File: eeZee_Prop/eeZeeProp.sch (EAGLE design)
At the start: 33 parts, among them Q1 5MHz, Q2 2N3904SMD, SW1 RESET, U1 P8X32A-Q44, U2 24LC256-I/ST, U3 NCP1117 3V3

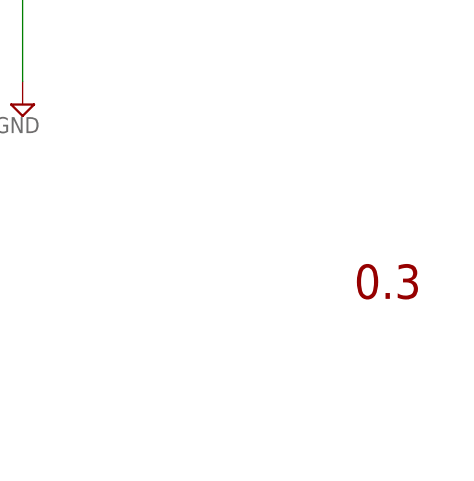
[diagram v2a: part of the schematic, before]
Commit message: Enlarged pads for SOT-23 and SOD123F for easier hand assembly. Slight tweaks to traces.
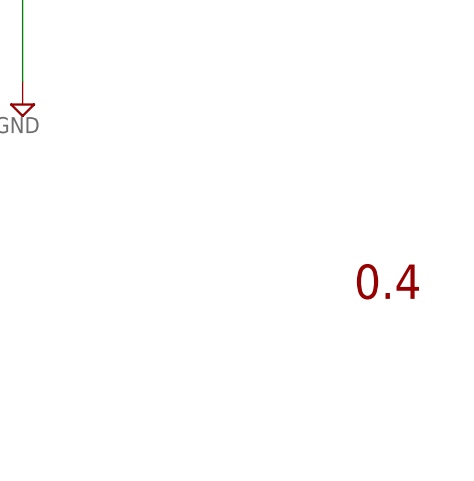
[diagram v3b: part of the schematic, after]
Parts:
- C7: PARTNO (none) -> 0603YC104KAT2A
- Q2: PARTNO (none) -> MMBT3904LT3G
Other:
- note added: "0.4"
- note removed: "0.3"
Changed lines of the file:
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@@
 <grid distance="0.1" unitdist="inch" unit="inch" style="lines" multiple="1" display="no" altdistance="0.01" altunitdist="inch" altunit="inch"/>
 <layers>
-<layer number="1" name="Top" color="4" fill="1" visible="yes" active="no"/>
-<layer number="16" name="Bottom" color="1" fill="1" visible="yes" active="no"/>
-<layer number="17" name="Pads" color="2" fill="1" visible="yes" active="no"/>
-<layer number="18" name="Vias" color="2" fill="1" visible="yes" active="no"/>
-<layer number="19" name="Unrouted" color="6" fill="1" visible="yes" active="no"/>
-<layer number="20" name="Dimension" color="15" fill="1" visible="yes" active="no"/>
-<layer number="21" name="tPlace" color="7" fill="1" visible="yes" active="no"/>
-<layer number="22" name="bPlace" color="7" fill="1" visible="yes" active="no"/>
-<layer number="23" name="tOrigins" color="15" fill="1" visible="yes" active="no"/>
-<layer number="24" name="bOrigins" color="15" fill="1" visible="yes" active="no"/>
-<layer number="25" name="tNames" color="7" fill="1" visible="yes" active="no"/>
-<layer number="26" name="bNames" color="7" fill="1" visible="yes" active="no"/>
-<layer number="27" name="tValues" color="7" fill="1" visible="yes" active="no"/>
-<layer number="28" name="bValues" color="7" fill="1" visible="yes" active="no"/>
+<layer number="1" name="Top" color="4" fill="1" visible="no" active="no"/>
+<layer number="16" name="Bottom" color="1" fill="1" visible="no" active="no"/>
+<layer number="17" name="Pads" color="2" fill="1" visible="no" active="no"/>
+<layer number="18" name="Vias" color="2" fill="1" visible="no" active="no"/>
+<layer number="19" name="Unrouted" color="6" fill="1" visible="no" active="no"/>
+<layer number="20" name="Dimension" color="15" fill="1" visible="no" active="no"/>
+<layer number="21" name="tPlace" color="7" fill="1" visible="no" active="no"/>
+<layer number="22" name="bPlace" color="7" fill="1" visible="no" active="no"/>
+<layer number="23" name="tOrigins" color="15" fill="1" visible="no" active="no"/>
+<layer number="24" name="bOrigins" color="15" fill="1" visible="no" active="no"/>
+<layer number="25" name="tNames" color="7" fill="1" visible="no" active="no"/>
+<layer number="26" name="bNames" color="7" fill="1" visible="no" active="no"/>
+<layer number="27" name="tValues" color="7" fill="1" visible="no" active="no"/>
+<layer number="28" name="bValues" color="7" fill="1" visible="no" active="no"/>
 <layer number="29" name="tStop" color="7" fill="3" visible="no" active="no"/>
 <layer number="30" name="bStop" color="7" fill="6" visible="no" active="no"/>
@@
 <layer number="35" name="tGlue" color="7" fill="4" visible="no" active="no"/>
 <layer number="36" name="bGlue" color="7" fill="5" visible="no" active="no"/>
-<layer number="37" name="tTest" color="7" fill="1" visible="yes" active="no"/>
-<layer number="38" name="bTest" color="7" fill="1" visible="yes" active="no"/>
+<layer number="37" name="tTest" color="7" fill="1" visible="no" active="no"/>
+<layer number="38" name="bTest" color="7" fill="1" visible="no" active="no"/>
 <layer number="39" name="tKeepout" color="4" fill="11" visible="no" active="no"/>
 <layer number="40" name="bKeepout" color="1" fill="11" visible="no" active="no"/>
@@
 <layer number="44" name="Drills" color="7" fill="1" visible="no" active="no"/>
 <layer number="45" name="Holes" color="7" fill="1" visible="no" active="no"/>
-<layer number="46" name="Milling" color="3" fill="1" visible="yes" active="no"/>
-<layer number="47" name="Measures" color="7" fill="1" visible="yes" active="no"/>
-<layer number="48" name="Document" color="7" fill="1" visible="yes" active="no"/>
-<layer number="49" name="Reference" color="7" fill="1" visible="yes" active="no"/>
-<layer number="50" name="dxf" color="7" fill="1" visible="yes" active="no"/>
-<layer number="51" name="tDocu" color="7" fill="1" visible="yes" active="no"/>
-<layer number="52" name="bDocu" color="7" fill="1" visible="yes" active="no"/>
-<layer number="53" name="tGND_GNDA" color="7" fill="9" visible="yes" active="no"/>
-<layer number="54" name="bGND_GNDA" color="1" fill="9" visible="yes" active="no"/>
-<layer number="56" name="wert" color="7" fill="1" visible="yes" active="no"/>
+<layer number="46" name="Milling" color="3" fill="1" visible="no" active="no"/>
+<layer number="47" name="Measures" color="7" fill="1" visible="no" active="no"/>
+<layer number="48" name="Document" color="7" fill="1" visible="no" active="no"/>
+<layer number="49" name="Reference" color="7" fill="1" visible="no" active="no"/>
+<layer number="50" name="dxf" color="7" fill="1" visible="no" active="no"/>
+<layer number="51" name="tDocu" color="7" fill="1" visible="no" active="no"/>
+<layer number="52" name="bDocu" color="7" fill="1" visible="no" active="no"/>
+<layer number="53" name="tGND_GNDA" color="7" fill="9" visible="no" active="no"/>
+<layer number="54" name="bGND_GNDA" color="1" fill="9" visible="no" active="no"/>
+<layer number="56" name="wert" color="7" fill="1" visible="no" active="no"/>
 <layer number="91" name="Nets" color="2" fill="1" visible="yes" active="yes"/>
 <layer number="92" name="Busses" color="1" fill="1" visible="yes" active="yes"/>
@@
 </part>
 <part name="SJ1" library="SparkFun" deviceset="SOLDERJUMPER" device="NO" value="BYPASS"/>
-<part name="Q2" library="mes_transistors" deviceset="2N3904" device="SMD"/>
+<part name="Q2" library="mes_transistors" deviceset="2N3904" device="SMD">
+<attribute name="PARTNO" value="MMBT3904LT3G"/>
+</part>
 <part name="R8" library="rcl" deviceset="R-US_" device="R0603" value="10k">
 <attribute name="PARTNO" value="ERJ-3GEYJ103V"/>
@@
 <attribute name="TOL" value="5%"/>
 </part>
-<part name="C7" library="rcl" deviceset="C-US" device="C0603" value="0.1uF"/>
+<part name="C7" library="rcl" deviceset="C-US" device="C0603" value="0.1uF">
+<attribute name="PARTNO" value="0603YC104KAT2A"/>
+</part>
 <part name="SUPPLY11" library="supply2" deviceset="GND" device=""/>
 <part name="SUPPLY6" library="supply2" deviceset="GND" device=""/>
@@
 <text x="43.18" y="48.26" size="1.778" layer="95">!BOE</text>
 <text x="161.29" y="24.13" size="3.81" layer="94">eeZeeProp</text>
-<text x="232.41" y="24.13" size="3.81" layer="94">0.3</text>
+<text x="232.41" y="24.13" size="3.81" layer="94">0.4</text>
 <text x="86.36" y="157.48" size="1.778" layer="97">RXI</text>
 <text x="86.36" y="154.94" size="1.778" layer="97">TXO</text>
@@
 </instance>
 <instance part="SJ1" gate="1" x="127" y="157.48" rot="R180"/>
-<instance part="Q2" gate="G1" x="193.04" y="63.5"/>
+<instance part="Q2" gate="G1" x="193.04" y="63.5">
+<attribute name="PARTNO" x="193.04" y="63.5" size="1.778" layer="96" display="off"/>
+</instance>
 <instance part="R8" gate="G$1" x="180.34" y="55.88" rot="R90">
 <attribute name="PARTNO" value="ERJ-3GEYJ103V" x="180.34" y="55.88" size="1.778" layer="96" display="off"/>
@@
 <attribute name="TOL" x="180.34" y="55.88" size="1.778" layer="96" rot="R90" display="off"/>
 </instance>
-<instance part="C7" gate="G$1" x="170.18" y="63.5" rot="R270"/>
+<instance part="C7" gate="G$1" x="170.18" y="63.5" rot="R270">
+<attribute name="PARTNO" x="170.18" y="63.5" size="1.778" layer="96" display="off"/>
+</instance>
 <instance part="SUPPLY11" gate="GND" x="180.34" y="45.72" rot="MR0"/>
 <instance part="SUPPLY6" gate="GND" x="195.58" y="45.72" rot="MR0"/>

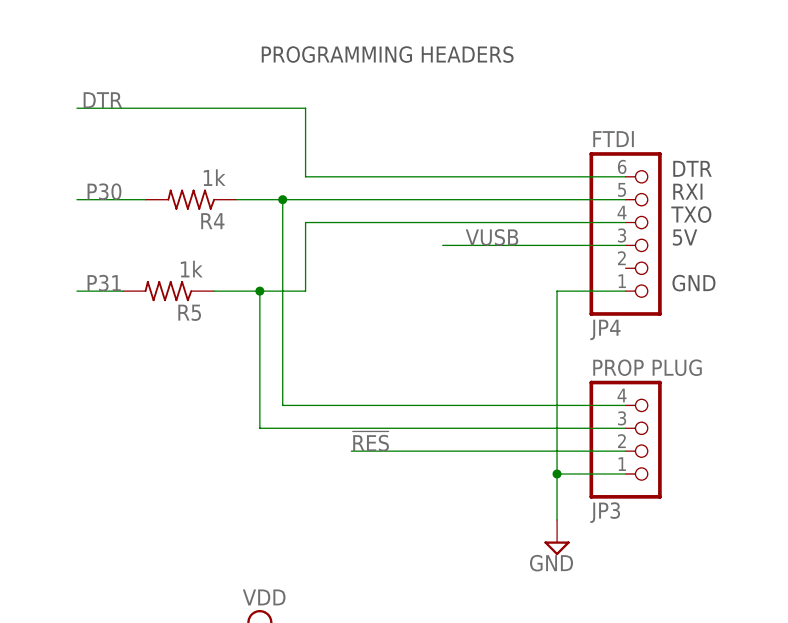
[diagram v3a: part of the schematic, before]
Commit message: Version 0.4, changes some footprints for easier rework, some mods to routing, mitered corners, some other stuff I'm forgetting.
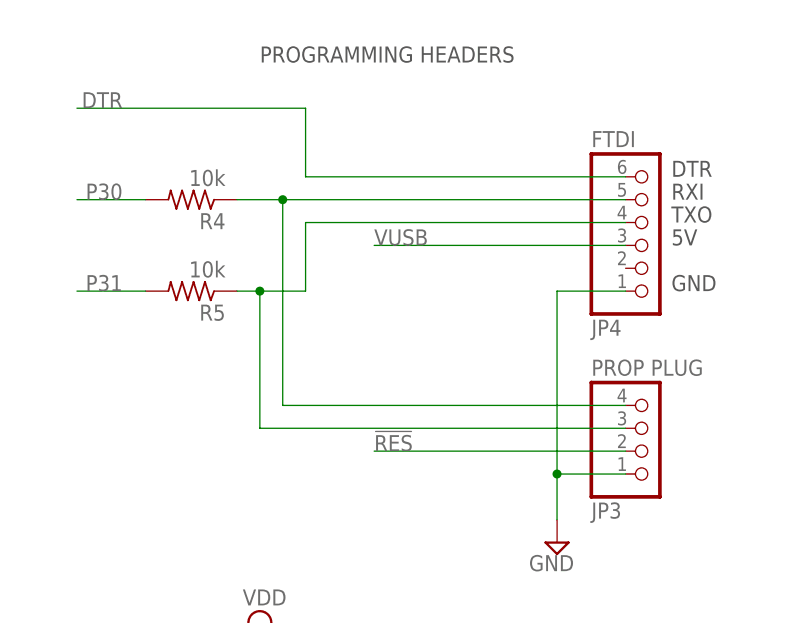
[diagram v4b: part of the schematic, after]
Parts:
- R4, R5: value 1k -> 10k
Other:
- moved on the sheet: R5
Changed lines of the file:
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@@
 <?xml version="1.0" encoding="utf-8"?>
 <!DOCTYPE eagle SYSTEM "eagle.dtd">
-<eagle version="6.3">
+<eagle version="6.4">
 <drawing>
 <settings>
@@
 <grid distance="0.1" unitdist="inch" unit="inch" style="lines" multiple="1" display="no" altdistance="0.01" altunitdist="inch" altunit="inch"/>
 <layers>
-<layer number="1" name="Top" color="4" fill="1" visible="no" active="no"/>
-<layer number="16" name="Bottom" color="1" fill="1" visible="no" active="no"/>
-<layer number="17" name="Pads" color="2" fill="1" visible="no" active="no"/>
-<layer number="18" name="Vias" color="2" fill="1" visible="no" active="no"/>
-<layer number="19" name="Unrouted" color="6" fill="1" visible="no" active="no"/>
-<layer number="20" name="Dimension" color="15" fill="1" visible="no" active="no"/>
-<layer number="21" name="tPlace" color="7" fill="1" visible="no" active="no"/>
-<layer number="22" name="bPlace" color="7" fill="1" visible="no" active="no"/>
-<layer number="23" name="tOrigins" color="15" fill="1" visible="no" active="no"/>
-<layer number="24" name="bOrigins" color="15" fill="1" visible="no" active="no"/>
-<layer number="25" name="tNames" color="7" fill="1" visible="no" active="no"/>
-<layer number="26" name="bNames" color="7" fill="1" visible="no" active="no"/>
-<layer number="27" name="tValues" color="7" fill="1" visible="no" active="no"/>
-<layer number="28" name="bValues" color="7" fill="1" visible="no" active="no"/>
+<layer number="1" name="Top" color="4" fill="1" visible="yes" active="no"/>
+<layer number="16" name="Bottom" color="1" fill="1" visible="yes" active="no"/>
+<layer number="17" name="Pads" color="2" fill="1" visible="yes" active="no"/>
+<layer number="18" name="Vias" color="2" fill="1" visible="yes" active="no"/>
+<layer number="19" name="Unrouted" color="6" fill="1" visible="yes" active="no"/>
+<layer number="20" name="Dimension" color="15" fill="1" visible="yes" active="no"/>
+<layer number="21" name="tPlace" color="7" fill="1" visible="yes" active="no"/>
+<layer number="22" name="bPlace" color="7" fill="1" visible="yes" active="no"/>
+<layer number="23" name="tOrigins" color="15" fill="1" visible="yes" active="no"/>
+<layer number="24" name="bOrigins" color="15" fill="1" visible="yes" active="no"/>
+<layer number="25" name="tNames" color="7" fill="1" visible="yes" active="no"/>
+<layer number="26" name="bNames" color="7" fill="1" visible="yes" active="no"/>
+<layer number="27" name="tValues" color="7" fill="1" visible="yes" active="no"/>
+<layer number="28" name="bValues" color="7" fill="1" visible="yes" active="no"/>
 <layer number="29" name="tStop" color="7" fill="3" visible="no" active="no"/>
 <layer number="30" name="bStop" color="7" fill="6" visible="no" active="no"/>
@@
 <layer number="35" name="tGlue" color="7" fill="4" visible="no" active="no"/>
 <layer number="36" name="bGlue" color="7" fill="5" visible="no" active="no"/>
-<layer number="37" name="tTest" color="7" fill="1" visible="no" active="no"/>
-<layer number="38" name="bTest" color="7" fill="1" visible="no" active="no"/>
+<layer number="37" name="tTest" color="7" fill="1" visible="yes" active="no"/>
+<layer number="38" name="bTest" color="7" fill="1" visible="yes" active="no"/>
 <layer number="39" name="tKeepout" color="4" fill="11" visible="no" active="no"/>
 <layer number="40" name="bKeepout" color="1" fill="11" visible="no" active="no"/>
@@
 <layer number="44" name="Drills" color="7" fill="1" visible="no" active="no"/>
 <layer number="45" name="Holes" color="7" fill="1" visible="no" active="no"/>
-<layer number="46" name="Milling" color="3" fill="1" visible="no" active="no"/>
-<layer number="47" name="Measures" color="7" fill="1" visible="no" active="no"/>
-<layer number="48" name="Document" color="7" fill="1" visible="no" active="no"/>
-<layer number="49" name="Reference" color="7" fill="1" visible="no" active="no"/>
-<layer number="50" name="dxf" color="7" fill="1" visible="no" active="no"/>
-<layer number="51" name="tDocu" color="7" fill="1" visible="no" active="no"/>
-<layer number="52" name="bDocu" color="7" fill="1" visible="no" active="no"/>
-<layer number="53" name="tGND_GNDA" color="7" fill="9" visible="no" active="no"/>
-<layer number="54" name="bGND_GNDA" color="1" fill="9" visible="no" active="no"/>
-<layer number="56" name="wert" color="7" fill="1" visible="no" active="no"/>
+<layer number="46" name="Milling" color="3" fill="1" visible="yes" active="no"/>
+<layer number="47" name="Measures" color="7" fill="1" visible="yes" active="no"/>
+<layer number="48" name="Document" color="7" fill="1" visible="yes" active="no"/>
+<layer number="49" name="Reference" color="7" fill="1" visible="yes" active="no"/>
+<layer number="50" name="dxf" color="7" fill="1" visible="yes" active="no"/>
+<layer number="51" name="tDocu" color="7" fill="1" visible="yes" active="no"/>
+<layer number="52" name="bDocu" color="7" fill="1" visible="yes" active="no"/>
+<layer number="53" name="tGND_GNDA" color="7" fill="9" visible="yes" active="no"/>
+<layer number="54" name="bGND_GNDA" color="1" fill="9" visible="yes" active="no"/>
+<layer number="56" name="wert" color="7" fill="1" visible="yes" active="no"/>
 <layer number="91" name="Nets" color="2" fill="1" visible="yes" active="yes"/>
 <layer number="92" name="Busses" color="1" fill="1" visible="yes" active="yes"/>
@@
 </part>
 <part name="JP3" library="pinhead-2" deviceset="PINHD-1X04" device="_2.54-S" value="PROP PLUG"/>
-<part name="R4" library="rcl" deviceset="R-US_" device="R0603" value="1k">
+<part name="R4" library="rcl" deviceset="R-US_" device="R0603" value="10k">
 <attribute name="PARTNO" value="RC0603JR-071KL"/>
 <attribute name="RATE" value="100mW"/>
@@
 <attribute name="TOL" value="5%"/>
 </part>
-<part name="R5" library="rcl" deviceset="R-US_" device="R0603" value="1k">
+<part name="R5" library="rcl" deviceset="R-US_" device="R0603" value="10k">
 <attribute name="PARTNO" value="RC0603JR-071KL"/>
 <attribute name="RATE" value="100mW"/>
@@
 <attribute name="TOL" x="33.02" y="157.48" size="1.778" layer="96" rot="R180" display="off"/>
 </instance>
-<instance part="R5" gate="G$1" x="30.48" y="147.32" rot="R180">
-<attribute name="PARTNO" value="RC0603JR-071KL" x="30.48" y="147.32" size="1.778" layer="96" rot="R90" display="off"/>
-<attribute name="SIZE" x="30.48" y="147.32" size="1.778" layer="96" rot="R90" display="off"/>
-<attribute name="RATE" x="30.48" y="147.32" size="1.778" layer="96" rot="R180" display="off"/>
-<attribute name="TOL" x="30.48" y="147.32" size="1.778" layer="96" rot="R180" display="off"/>
+<instance part="R5" gate="G$1" x="33.02" y="147.32" rot="R180">
+<attribute name="PARTNO" value="RC0603JR-071KL" x="33.02" y="147.32" size="1.778" layer="96" rot="R90" display="off"/>
+<attribute name="SIZE" x="33.02" y="147.32" size="1.778" layer="96" rot="R90" display="off"/>
+<attribute name="RATE" x="33.02" y="147.32" size="1.778" layer="96" rot="R180" display="off"/>
+<attribute name="TOL" x="33.02" y="147.32" size="1.778" layer="96" rot="R180" display="off"/>
 </instance>
 <instance part="JP5" gate="A" x="15.24" y="73.66" rot="MR0"/>
@@
 <segment>
 <pinref part="JP3" gate="A" pin="2"/>
-<wire x1="81.28" y1="129.54" x2="50.8" y2="129.54" width="0.1524" layer="91"/>
-<label x="50.8" y="129.54" size="1.778" layer="95"/>
+<wire x1="81.28" y1="129.54" x2="53.34" y2="129.54" width="0.1524" layer="91"/>
+<label x="53.34" y="129.54" size="1.778" layer="95"/>
 </segment>
 <segment>
@@
 <segment>
 <pinref part="R5" gate="G$1" pin="2"/>
-<wire x1="20.32" y1="147.32" x2="25.4" y2="147.32" width="0.1524" layer="91"/>
+<wire x1="20.32" y1="147.32" x2="27.94" y2="147.32" width="0.1524" layer="91"/>
 <label x="25.4" y="147.32" size="1.778" layer="95" rot="MR0"/>
 </segment>
@@
 <pinref part="JP4" gate="A" pin="4"/>
 <pinref part="R5" gate="G$1" pin="1"/>
-<wire x1="35.56" y1="147.32" x2="40.64" y2="147.32" width="0.1524" layer="91"/>
+<wire x1="38.1" y1="147.32" x2="40.64" y2="147.32" width="0.1524" layer="91"/>
 <pinref part="JP3" gate="A" pin="3"/>
 <wire x1="40.64" y1="147.32" x2="45.72" y2="147.32" width="0.1524" layer="91"/>
@@
 <segment>
 <pinref part="JP4" gate="A" pin="3"/>
-<wire x1="81.28" y1="152.4" x2="60.96" y2="152.4" width="0.1524" layer="91"/>
-<label x="63.5" y="152.4" size="1.778" layer="95"/>
-</segment>
-<segment>
+<wire x1="81.28" y1="152.4" x2="53.34" y2="152.4" width="0.1524" layer="91"/>
+<label x="53.34" y="152.4" size="1.778" layer="95"/>
+</segment>
+<segment>
